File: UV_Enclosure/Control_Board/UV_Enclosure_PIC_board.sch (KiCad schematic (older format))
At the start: 6 parts

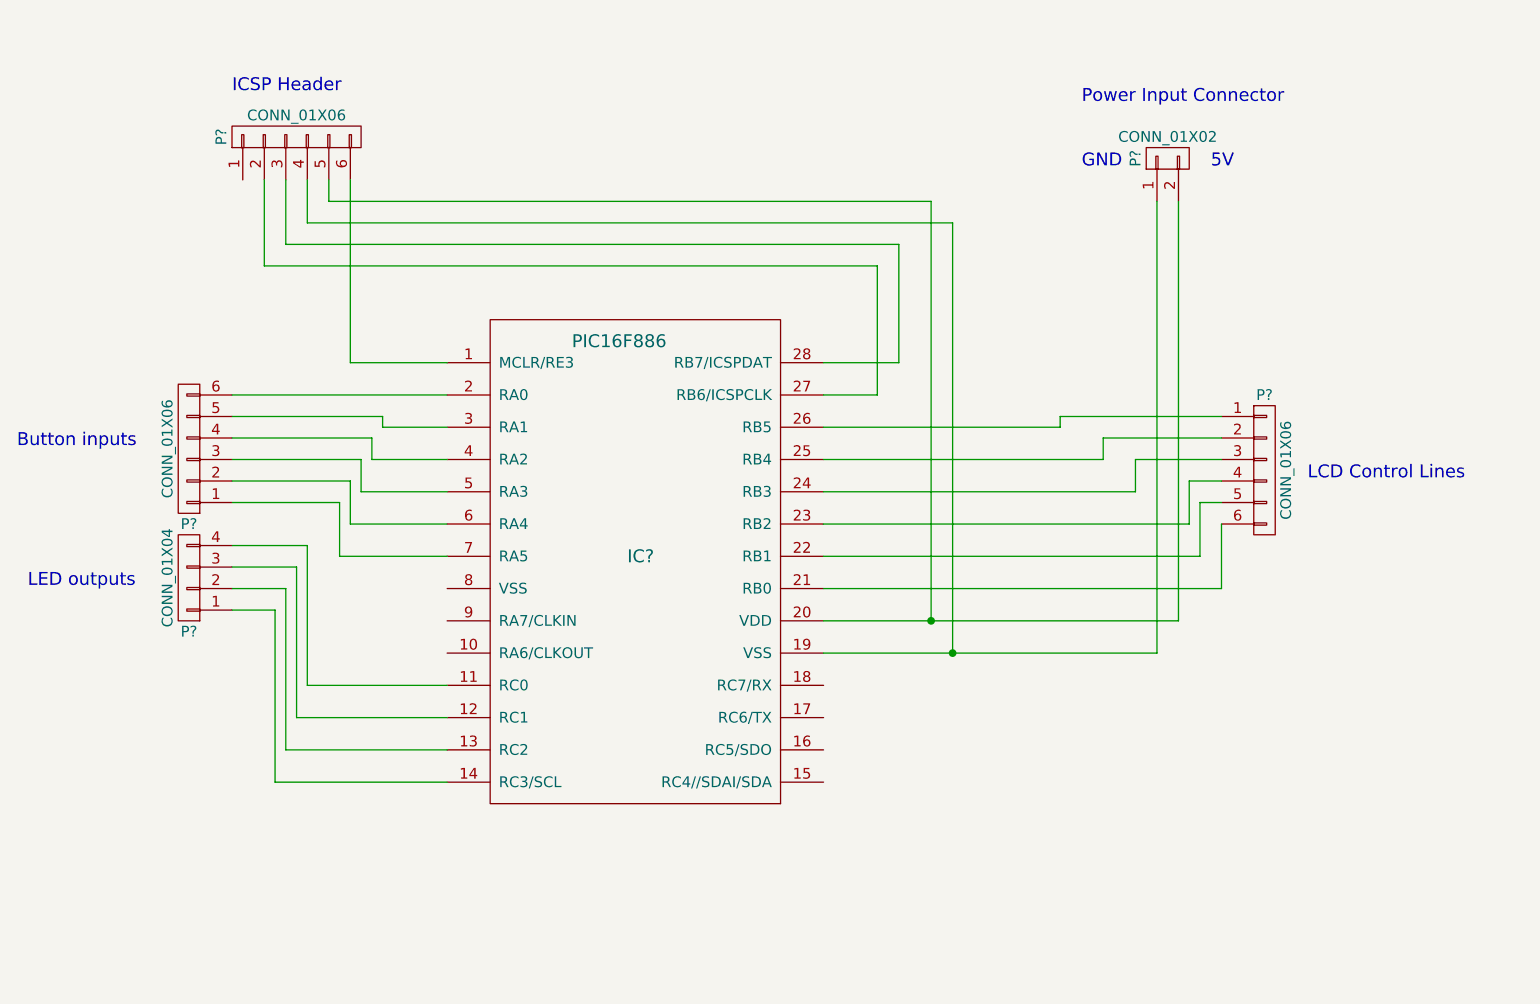
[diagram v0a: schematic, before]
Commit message: Updated schematic for control board
Updated the schematic for the new control board with new PIC (PIC18F45K50). This was changed due to the original PIC having non-functioning pins on PORTB.
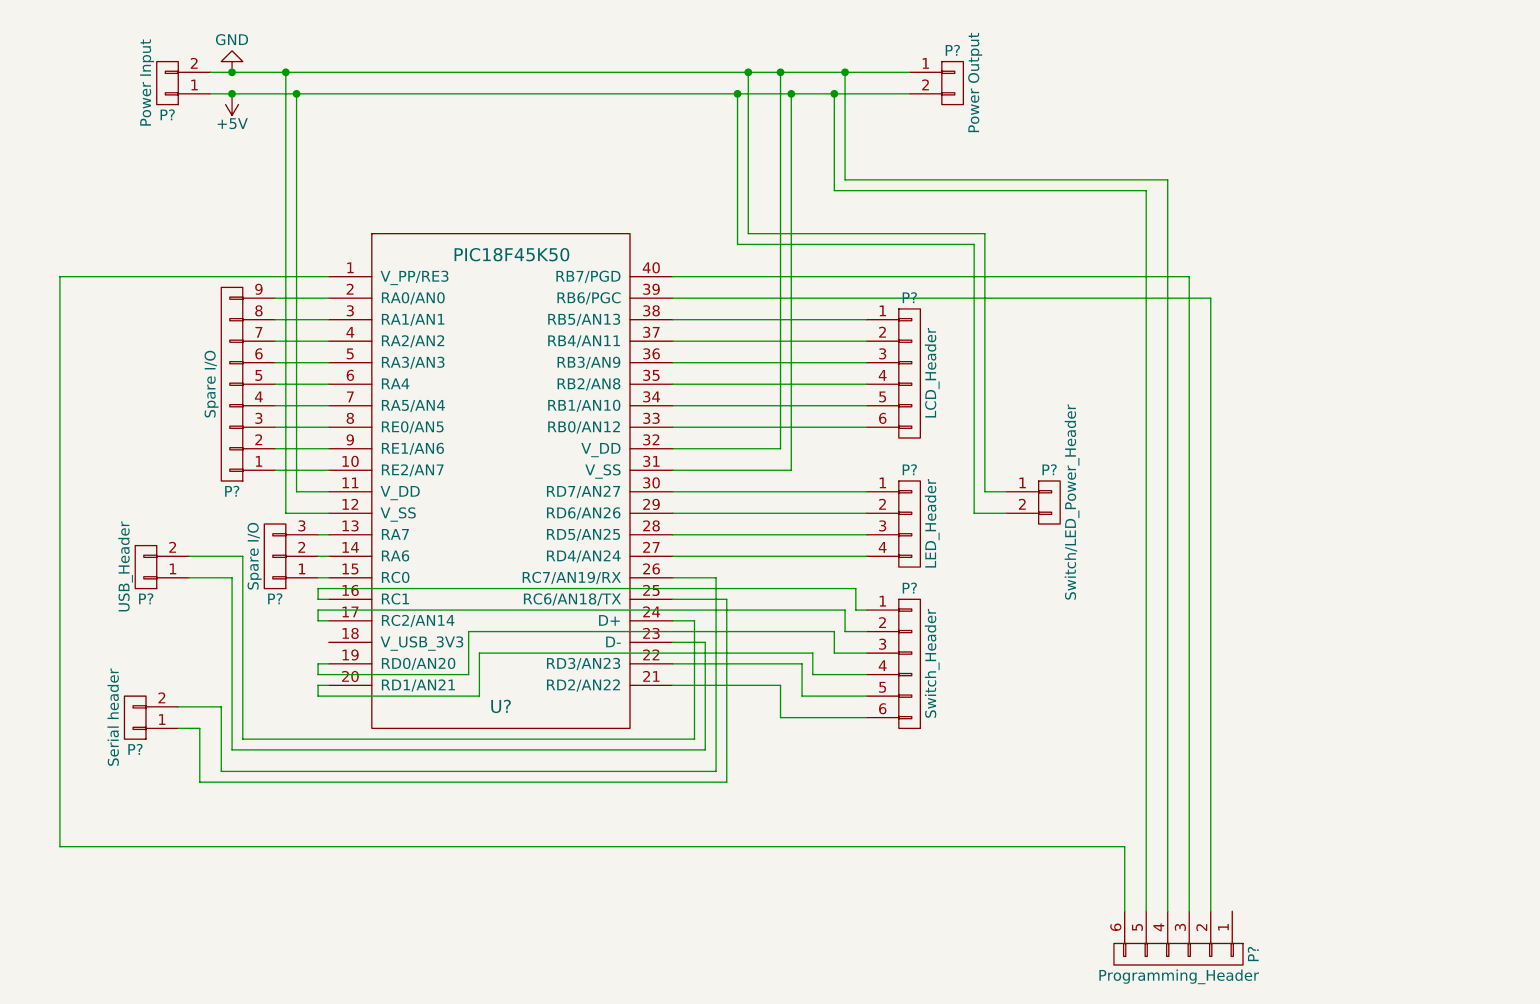
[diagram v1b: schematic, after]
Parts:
- removed IC?: PIC16F886, symbol PIC16F886
- removed P? (x3): CONN_01X06, symbol CONN_01X06
- removed P?: CONN_01X02, symbol CONN_01X02
- removed P?: CONN_01X04, symbol CONN_01X04
- added P?: Programming_Header, symbol CONN_01X06
- added P?: LCD_Header, symbol CONN_01X06
- added P?: LED_Header, symbol CONN_01X04
- added P?: Switch_Header, symbol CONN_01X06
- added P?: Switch/LED_Power_Header, symbol CONN_01X02
- added P?: Serial header, symbol CONN_01X02
- added P?: USB_Header, symbol CONN_01X02
- added P?: Power Input, symbol CONN_01X02
- added P?: Power Output, symbol CONN_01X02
- added P?: Spare I/O, symbol CONN_01X03
- added P?: Spare I/O, symbol CONN_01X09
- added U?: PIC18F45K50, symbol PIC18F45K50
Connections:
- new net: P?.6 (P6), U?.1 (V_PP/RE3)
- new net: P?.1 (P1), U?.10 (RE2/AN7)
- new net: P?.3 (P3), U?.13 (RA7)
- new net: P?.2 (P2), U?.14 (RA6)
- new net: P?.1 (P1), U?.15 (RC0)
- new net: P?.1 (P1), U?.16 (RC1)
- new net: P?.2 (P2), U?.17 (RC2/AN14)
- new net: P?.3 (P3), U?.19 (RD0/AN20)
- new net: P?.9 (P9), U?.2 (RA0/AN0)
- new net: P?.4 (P4), U?.20 (RD1/AN21)
- new net: P?.6 (P6), U?.21 (RD2/AN22)
- new net: P?.5 (P5), U?.22 (RD3/AN23)
- new net: P?.1 (P1), U?.23 (D-)
- new net: P?.2 (P2), U?.24 (D+)
- new net: P?.1 (P1), U?.25 (RC6/AN18/TX)
- new net: P?.2 (P2), U?.26 (RC7/AN19/RX)
- new net: P?.4 (P4), U?.27 (RD4/AN24)
- new net: P?.3 (P3), U?.28 (RD5/AN25)
- new net: P?.2 (P2), U?.29 (RD6/AN26)
- new net: P?.8 (P8), U?.3 (RA1/AN1)
- new net: P?.1 (P1), U?.30 (RD7/AN27)
- new net: P?.6 (P6), U?.33 (RB0/AN12)
- new net: P?.5 (P5), U?.34 (RB1/AN10)
- new net: P?.4 (P4), U?.35 (RB2/AN8)
- new net: P?.3 (P3), U?.36 (RB3/AN9)
- new net: P?.2 (P2), U?.37 (RB4/AN11)
- new net: P?.1 (P1), U?.38 (RB5/AN13)
- new net: P?.2 (P2), U?.39 (RB6/PGC)
- new net: P?.7 (P7), U?.4 (RA2/AN2)
- new net: P?.3 (P3), U?.40 (RB7/PGD)
- new net: P?.6 (P6), U?.5 (RA3/AN3)
- new net: P?.5 (P5), U?.6 (RA4)
- new net: P?.4 (P4), U?.7 (RA5/AN4)
- new net: P?.3 (P3), U?.8 (RE0/AN5)
- new net: P?.2 (P2), U?.9 (RE1/AN6)
- new net +5V: P?.1 (P1), P?.2 (P2), P?.2 (P2), P?.5 (P5), U?.11 (V_DD), U?.31 (V_SS)
- new net GND: P?.1 (P1), P?.1 (P1), P?.2 (P2), P?.4 (P4), U?.12 (V_SS), U?.32 (V_DD)
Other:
- note removed: "5V"
- note removed: "Button inputs"
- note removed: "GND"
- note removed: "ICSP Header"
- note removed: "LCD Control Lines"
- note removed: "LED outputs"
- note removed: "Power Input Connector"
